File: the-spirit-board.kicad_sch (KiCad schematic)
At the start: 60 parts, among them IC1 ESP32-C6-WROOM-1-N8, IC2 AP2112K-3.3TRG1, IC3 ICS-43434, J1 RAHUC31AUTR, Q1 BSS138, Q2 BSS138, Q3 BSS138, Q4 BSS138, Q5 BSS138, Q6 BSS138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

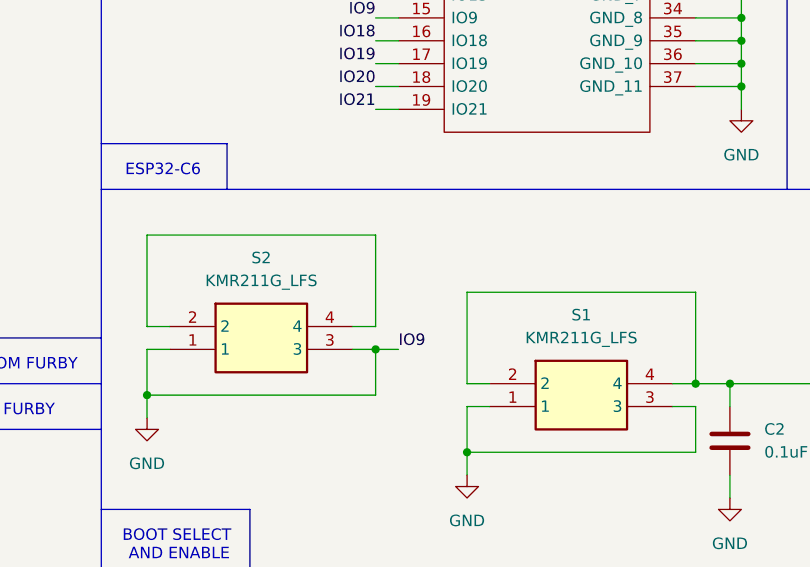
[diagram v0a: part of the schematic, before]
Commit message: Lots of updates to the PCB; all connections made except for one diode; working on passing DRC; targeting 4pcb
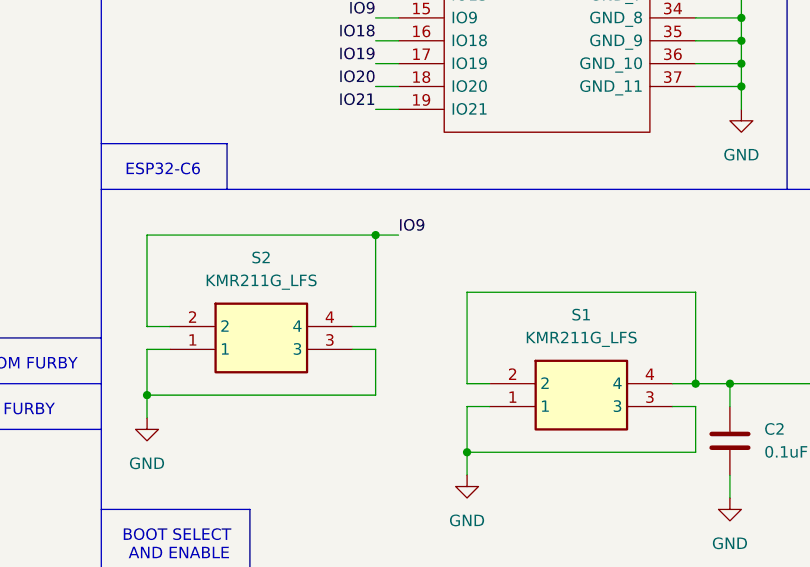
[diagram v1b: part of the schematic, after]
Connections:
- net GND: no longer IC1.15 (IO9), Q7.2 (S), R27.2
- net IO9: now reaches S2.2, S2.4
- net IO9: now also IC1.15 (IO9), Q7.2 (S), R27.2
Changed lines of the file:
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@@
 	)
 	(junction
+		(at 133.35 85.09)
+		(diameter 0)
+		(color 0 0 0 0)
+	)
+	(junction
 		(at 77.47 138.43)
 		(diameter 0)
@@
 	)
 	(junction
-		(at 57.15 191.77)
+		(at 20.32 223.52)
 		(diameter 0)
 		(color 0 0 0 0)
 	)
 	(junction
-		(at 173.99 63.5)
+		(at 57.15 191.77)
 		(diameter 0)
 		(color 0 0 0 0)
 	)
 	(junction
-		(at 133.35 97.79)
+		(at 173.99 63.5)
 		(diameter 0)
 		(color 0 0 0 0)
@@
 	)
 	(junction
-		(at 20.32 223.52)
-		(diameter 0)
-		(color 0 0 0 0)
-	)
-	(junction
 		(at 29.21 97.79)
 		(diameter 0)
@@
 	(wire
 		(pts
+			(xy 17.78 223.52) (xy 20.32 223.52)
+		)
+		(stroke
+			(width 0)
+			(type default)
+		)
+	)
+	(wire
+		(pts
 			(xy 40.64 113.03) (xy 40.64 115.57)
 		)
@@
 	(wire
 		(pts
-			(xy 17.78 223.52) (xy 20.32 223.52)
-		)
-		(stroke
-			(width 0)
-			(type default)
-		)
-	)
-	(wire
-		(pts
 			(xy 109.22 27.94) (xy 109.22 22.86)
 		)
@@
 	(wire
 		(pts
-			(xy 133.35 97.79) (xy 135.89 97.79)
-		)
-		(stroke
-			(width 0)
-			(type default)
-		)
-	)
-	(wire
-		(pts
 			(xy 231.14 151.13) (xy 233.68 151.13)
 		)
@@
 	(wire
 		(pts
+			(xy 133.35 85.09) (xy 135.89 85.09)
+		)
+		(stroke
+			(width 0)
+			(type default)
+		)
+	)
+	(wire
+		(pts
 			(xy 133.35 60.96) (xy 135.89 60.96)
 		)
@@
 	)
 	(label "IO9"
-		(at 135.89 97.79 0)
+		(at 135.89 85.09 0)
 		(effects
 			(font

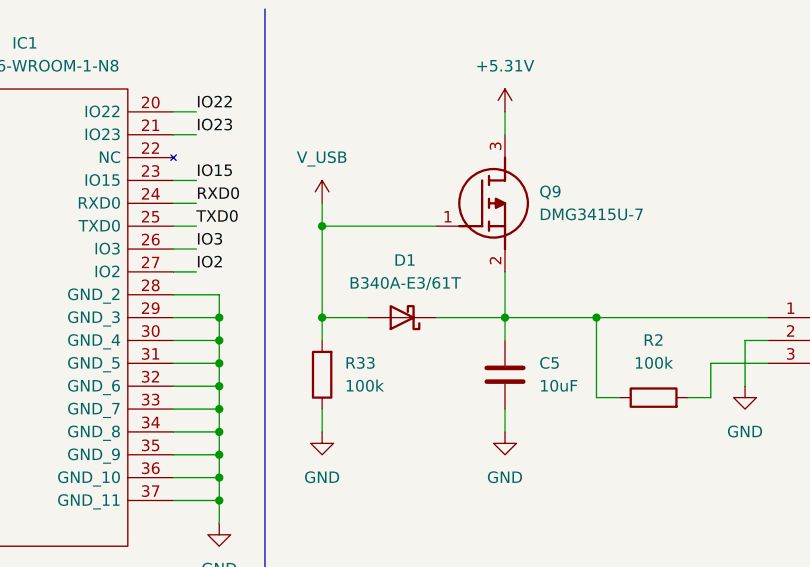
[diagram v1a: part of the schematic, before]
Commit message: Update the diode in the power supply
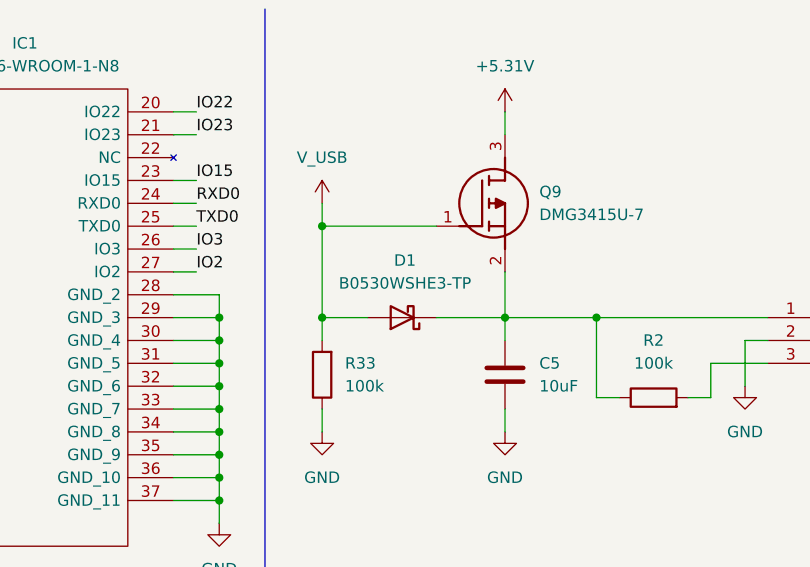
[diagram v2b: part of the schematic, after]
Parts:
- D1: value B340A-E3/61T -> B0530WSHE3-TP; footprint Diode_SMD:D_SMA -> Diode_SMD:D_SOD-323
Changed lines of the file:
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@@
 			)
 		)
-		(property "Value" "B340A-E3/61T"
+		(property "Value" "B0530WSHE3-TP"
 			(at 194.6275 44.45 0)
 			(effects
@@
 			)
 		)
-		(property "Footprint" "Diode_SMD:D_SMA"
+		(property "Footprint" "Diode_SMD:D_SOD-323"
 			(at 194.31 48.26 0)
 			(effects

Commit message: Update the schematic and layout after choosing parts
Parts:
- C1, C8: JLCPCB Part Number (none) -> C15849
- C2, C3: JLCPCB Part Number (none) -> C307331
- C4, C5, C6: footprint Capacitor_SMD:C_0603_1608Metric -> Capacitor_SMD:C_0805_2012Metric; JLCPCB Part Number (none) -> C440198
- C7: JLCPCB Part Number (none) -> C14663
- D1: JLCPCB Part Number (none) -> C3759178
- D2: JLCPCB Part Number (none) -> C2286
- IC1: JLCPCB Part Number (none) -> C5366877
- IC2: JLCPCB Part Number (none) -> C51118
- IC3: JLCPCB Part Number (none) -> C5656610
- J1: JLCPCB Part Number (none) -> C21350227
- Q1, Q2, Q3, Q4, Q5, Q6, Q7, Q8: JLCPCB Part Number (none) -> C52895
- Q9: JLCPCB Part Number (none) -> C96616
- R1, R29, R30, R34: JLCPCB Part Number (none) -> C23186
- R10, R11, R14, R15, R16, R17, R18, R19, R20, R21, R27, R28, R31, R32, R4: JLCPCB Part Number (none) -> C25804
- R12: JLCPCB Part Number (none) -> C25810
- R13: JLCPCB Part Number (none) -> C22984
- R2, R33: JLCPCB Part Number (none) -> C25803
- R22, R23, R24, R3, R8, R9: JLCPCB Part Number (none) -> C23162
- R25, R6: JLCPCB Part Number (none) -> C23018
- R26, R7: JLCPCB Part Number (none) -> C4260
- R5: JLCPCB Part Number (none) -> C4190
- S1, S2: JLCPCB Part Number (none) -> C221675
- U1: JLCPCB Part Number (none) -> N/A
